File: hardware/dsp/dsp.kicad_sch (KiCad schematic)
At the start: 24 parts, among them J1 Insert1, J2 Insert2, J3 Insert3, J4 Insert4, J5 Insert5, J6 Insert6, J7 Insert7, J8 Insert8

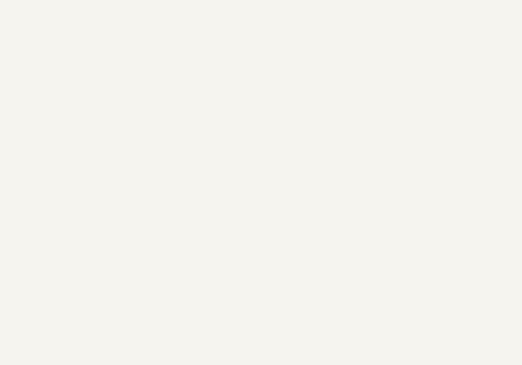
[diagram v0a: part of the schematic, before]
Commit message: Add barrel jack symbol and KiCad gitignore rules
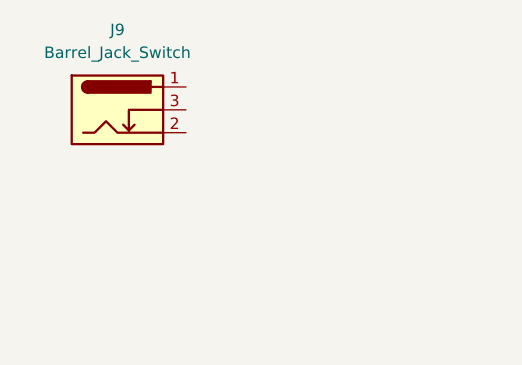
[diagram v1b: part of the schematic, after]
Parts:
- added J9: Barrel_Jack_Switch, symbol Connector:Barrel_Jack_Switch
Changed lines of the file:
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@@
+	)
+	(symbol
+		(lib_id "Connector:Barrel_Jack_Switch")
+		(at 144.78 27.94 0)
+		(unit 1)
+		(exclude_from_sim no)
+		(in_bom yes)
+		(on_board yes)
+		(dnp no)
+		(fields_autoplaced yes)
+		(property "Reference" "J9"
+			(at 144.78 19.05 0)
+			(effects
+				(font
+					(size 1.27 1.27)
+				)
+			)
+		)
+		(property "Value" "Barrel_Jack_Switch"
+			(at 144.78 21.59 0)
+			(effects
+				(font
+					(size 1.27 1.27)
+				)
+			)
+		)
+		(property "Footprint" ""
+			(at 146.05 28.956 0)
+			(effects
+				(font
+					(size 1.27 1.27)
+				)
+				(hide yes)
+			)
+		)
+		(property "Datasheet" "~"
+			(at 146.05 28.956 0)
+			(effects
+				(font
+					(size 1.27 1.27)
+				)
+				(hide yes)
+			)
+		)
+		(property "Description" "DC Barrel Jack with an internal switch"
+			(at 144.78 27.94 0)
+			(effects
+				(font
+					(size 1.27 1.27)
+				)
+				(hide yes)
+			)
+		)
+		(pin "1"
+		)
+		(pin "2"
+		)
+		(pin "3"
+		)
+		(instances
+			(project ""
+				(path "/830eff83-f012-43cb-96fd-a494f8ceadf0"
+					(reference "J9")
+					(unit 1)
+				)
+			)
+		)
 	)
 	(symbol
